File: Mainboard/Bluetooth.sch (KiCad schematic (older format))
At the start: 26 parts, among them J10 U.FL, J11 JST-PH 01x02, U10 BTM331

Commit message: Modify library references
As described in the README of the newly added libraries submodule.
Schematic and PCB are synced.

Hardware folder is renamed to mainboard
Any other PCBs can be put in their own subfolder in the gitrepo

Commit also swaps source/drain of Q1 because it appeared wrong for some
reason after updating all symbol/footprints.
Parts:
- J10: footprint ZOUDIOfootprints:Hirose_U.FL-R-SMT-1 -> ZOUDIO-footprints:Hirose_U.FL-R-SMT-1; symbol ZOUDIOsymbols:U.FL -> ZOUDIO-symbols:U.FL
- U10: footprint ZOUDIOfootprints:BTM331 -> ZOUDIO-footprints:BTM331; symbol ZOUDIOsymbols:BTM331 -> ZOUDIO-symbols:BTM331
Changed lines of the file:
@@
 $EndComp
 $Comp
-L ZOUDIOsymbols:BTM331 U10
+L ZOUDIO-symbols:BTM331 U10
 U 1 1 5FC5AF86
 P 4100 4100
+AR Path="/5FC5AF86" Ref="U10"  Part="1"
+AR Path="/60BB5CE1/5FC5AF86" Ref="U10"  Part="1"
 F 0 "U10" H 4100 4150 50  0000 C CNN
 F 1 "BTM331" H 4100 4050 50  0000 C CNN
-F 2 "ZOUDIOfootprints:BTM331" H 3650 4400 50  0001 C CNN
+F 2 "ZOUDIO-footprints:BTM331" H 3650 4400 50  0001 C CNN
 F 3 "" H 3650 4400 50  0001 C CNN
 F 4 "Tianjiarun" H 4100 4100 50  0001 C CNN "Manufacturer"
@@
 	2550 4850 2550 4900
 $Comp
-L ZOUDIOsymbols:U.FL J10
+L ZOUDIO-symbols:U.FL J10
 U 1 1 5FC5B37E
 P 3850 2350
 F 0 "J10" H 3850 2615 50  0000 C CNN
 F 1 "U.FL" H 3850 2524 50  0000 C CNN
-F 2 "ZOUDIOfootprints:Hirose_U.FL-R-SMT-1" H 3850 2350 50  0001 C CNN
+F 2 "ZOUDIO-footprints:Hirose_U.FL-R-SMT-1" H 3850 2350 50  0001 C CNN
 F 3 "" H 3850 2350 50  0001 C CNN
 F 4 "Hirose" H 3850 2350 50  0001 C CNN "Manufacturer"

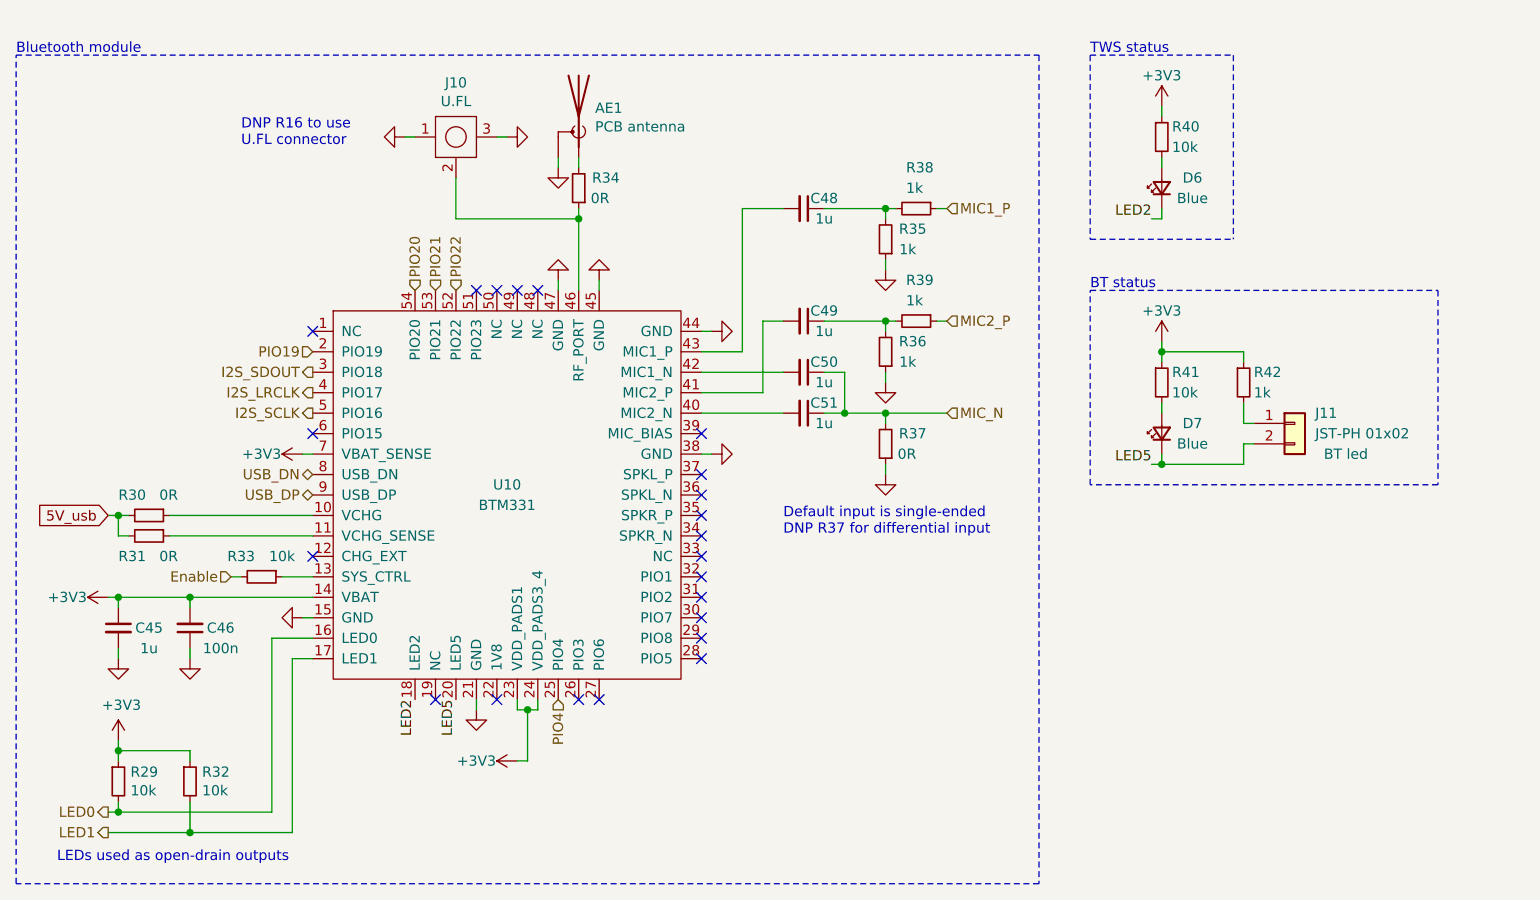
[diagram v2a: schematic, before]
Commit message: Before testing CH340B and VCHG
Cleaned up amp lay-out a bit in the meanwhile
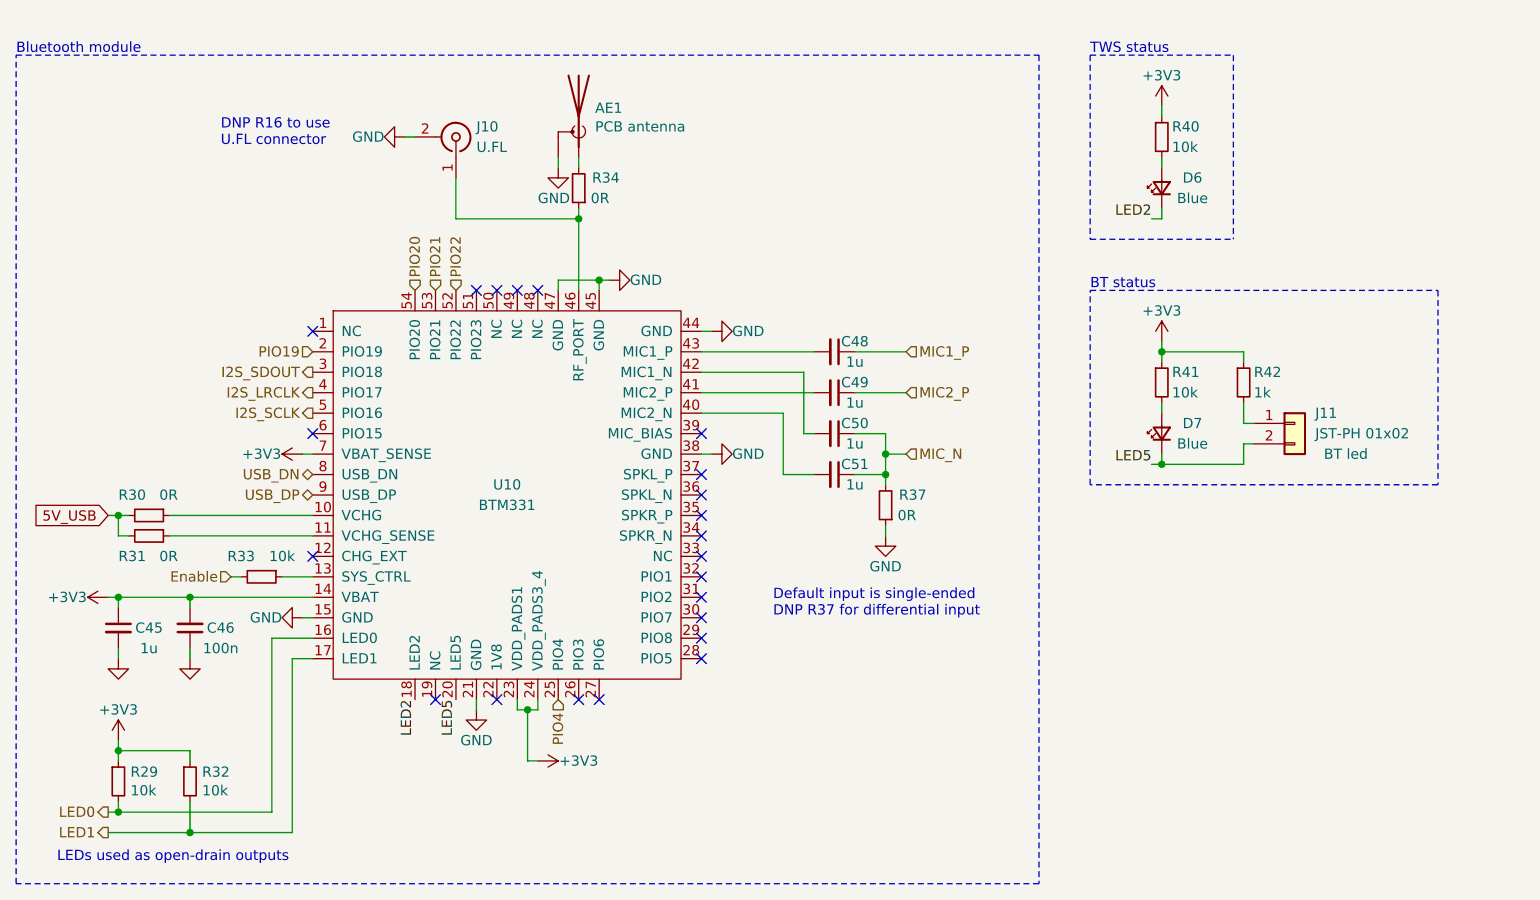
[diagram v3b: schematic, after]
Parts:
- removed J10: U.FL, ZOUDIO-footprints:Hirose_U.FL-R-SMT-1, symbol ZOUDIO-symbols:U.FL
- removed R35, R36, R38, R39: 1k, Resistor_SMD:R_0603_1608Metric, symbol Device:R_Small
- added J10: U.FL, Connector_Coaxial:U.FL_Hirose_U.FL-R-SMT-1_Vertical, symbol Connector:Conn_Coaxial
- AE1: Config DNP -> dnp; Partnumber virtual -> (none)
- C45, C48, C49, C50, C51: Manufacturer Yageo -> Taiyo Yuden; Partnumber CC0805KKX7R9BB105 -> UMK212B7105KG-T
- C46: Manufacturer Walsin -> Murata; Partnumber 0603B104J500CT -> GCM188L81H104KA57D
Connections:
- net GND: now also J10.2 (Ext)
- net MIC1_P: now also C48.1
- net MIC2_P: now also C49.1
- net at R34.1, U10.46 (RF_PORT): now also J10.1 (In)
- net 5V_usb renamed 5V_USB
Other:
- moved on the sheet: C48, C49, C50, C51, R37

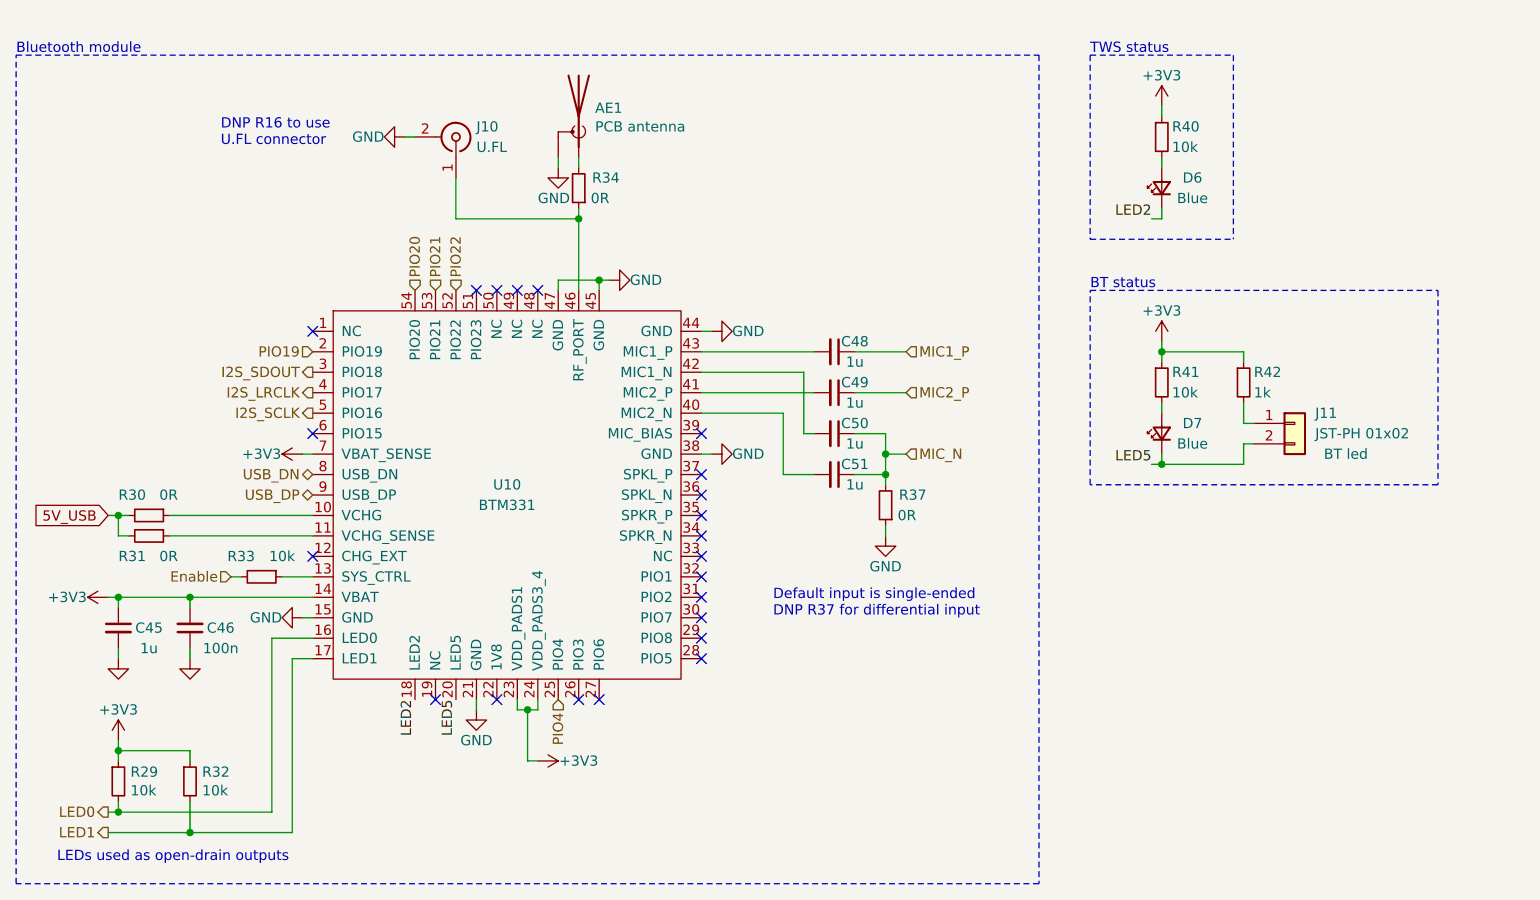
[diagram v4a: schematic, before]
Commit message: Mainboard: Version 1.0
Still need to clean up 3D models and BoM list,
but gerberexport-ready and ready to order.
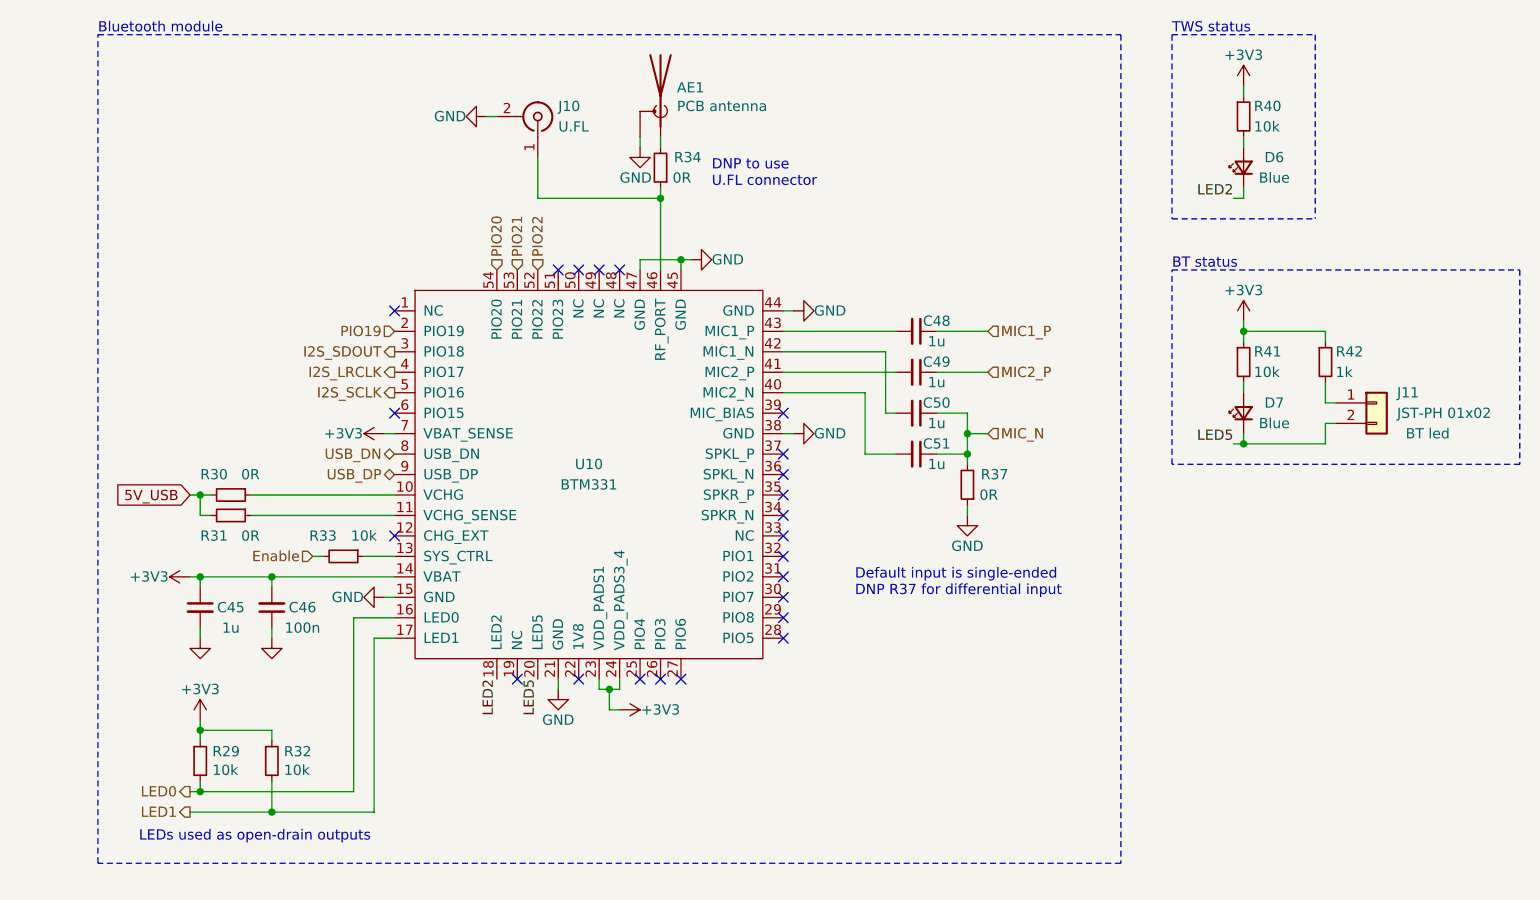
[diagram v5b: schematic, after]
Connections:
- net PIO4: no longer names the net of U10.25 (PIO4)
- no-connect marks 22 -> 23
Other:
- note added: "DNP to use \nU.FL connector"
- note removed: "DNP R16 to use \nU.FL connector"
- moved on the sheet: AE1, C45, C46, C48, C49, C50, C51, D6, D7, J10, J11, R29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

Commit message: Clean up schematic for BoM export
- Change 22u 0805's (amp decoupling) to 15u
- Change 680n 0805's (part of output filter) to 470n
- Change C1 (amp bulk cap) from 820u to 1000u
- Add BoM.ini for KiBom export and
- Complete fields needed for KiBom (Manufacturer and partnumber)
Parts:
- D6, D7: Manufacturer Orient -> Wurth; Partnumber ORH-B36G -> 150060BS75000
- J10: Manufacturer (none) -> Hirose; Partnumber (none) -> U.FL-R-SMT-1(10)
- J11: Manufacturer (none) -> JST; Partnumber (none) -> B2B-PH-K-S(LF)(SN)
- R29, R32, R33, R40, R41: Manufacturer Uni-royal -> Yageo; Partnumber 0603WAF1002T5E -> RC0603FR-0710KL
- R30, R31, R34, R37: Manufacturer Uni-royal -> Yageo; Partnumber 0603WAF0000T5E -> RC0603FR-070RL
- R42: Manufacturer Uni-royal -> Yageo; Partnumber 0603WAF1002T5E -> RC0603FR-071KL
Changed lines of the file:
@@
 F 2 "Resistor_SMD:R_0603_1608Metric" H 7700 3450 50  0001 C CNN
 F 3 "~" H 7700 3450 50  0001 C CNN
-F 4 "Uni-royal" H 7700 3450 50  0001 C CNN "Manufacturer"
-F 5 "0603WAF1002T5E" H 7700 3450 50  0001 C CNN "Partnumber"
+F 4 "Yageo" H 7700 3450 50  0001 C CNN "Manufacturer"
+F 5 "RC0603FR-0710KL" H 7700 3450 50  0001 C CNN "Partnumber"
 	1    7700 3450
 	1    0    0    -1
@@
 F 2 "LED_SMD:LED_0603_1608Metric" V 7700 3700 50  0001 C CNN
 F 3 "~" V 7700 3700 50  0001 C CNN
-F 4 "Orient" H 7700 3700 50  0001 C CNN "Manufacturer"
-F 5 "ORH-B36G" H 7700 3700 50  0001 C CNN "Partnumber"
+F 4 "Wurth" H 7700 3700 50  0001 C CNN "Manufacturer"
+F 5 "150060BS75000" H 7700 3700 50  0001 C CNN "Partnumber"
 	1    7700 3700
 	0    -1   -1   0
@@
 F 2 "Resistor_SMD:R_0603_1608Metric" H 4850 2500 50  0001 C CNN
 F 3 "~" H 4850 2500 50  0001 C CNN
-F 4 "Uni-royal" H 4850 2500 50  0001 C CNN "Manufacturer"
-F 5 "0603WAF0000T5E" H 4850 2500 50  0001 C CNN "Partnumber"
+F 4 "Yageo" H 4850 2500 50  0001 C CNN "Manufacturer"
+F 5 "RC0603FR-070RL" H 4850 2500 50  0001 C CNN "Partnumber"
 	1    4850 2500
 	-1   0    0    1
@@
 F 2 "Resistor_SMD:R_0603_1608Metric" H 7700 2250 50  0001 C CNN
 F 3 "~" H 7700 2250 50  0001 C CNN
-F 4 "Uni-royal" H 7700 2250 50  0001 C CNN "Manufacturer"
-F 5 "0603WAF1002T5E" H 7700 2250 50  0001 C CNN "Partnumber"
+F 4 "Yageo" H 7700 2250 50  0001 C CNN "Manufacturer"
+F 5 "RC0603FR-0710KL" H 7700 2250 50  0001 C CNN "Partnumber"
 	1    7700 2250
 	1    0    0    -1
@@
 F 2 "LED_SMD:LED_0603_1608Metric" V 7700 2500 50  0001 C CNN
 F 3 "~" V 7700 2500 50  0001 C CNN
-F 4 "Orient" H 7700 2500 50  0001 C CNN "Manufacturer"
-F 5 "ORH-B36G" H 7700 2500 50  0001 C CNN "Partnumber"
+F 4 "Wurth" H 7700 2500 50  0001 C CNN "Manufacturer"
+F 5 "150060BS75000" H 7700 2500 50  0001 C CNN "Partnumber"
 	1    7700 2500
 	0    -1   -1   0
@@
 F 2 "Resistor_SMD:R_0603_1608Metric" H 2600 5400 50  0001 C CNN
 F 3 "~" H 2600 5400 50  0001 C CNN
-F 4 "Uni-royal" H 2600 5400 50  0001 C CNN "Manufacturer"
-F 5 "0603WAF1002T5E" H 2600 5400 50  0001 C CNN "Partnumber"
+F 4 "Yageo" H 2600 5400 50  0001 C CNN "Manufacturer"
+F 5 "RC0603FR-0710KL" H 2600 5400 50  0001 C CNN "Partnumber"
 	1    2600 5400
 	1    0    0    -1
@@
 F 2 "Resistor_SMD:R_0603_1608Metric" H 2950 5400 50  0001 C CNN
 F 3 "~" H 2950 5400 50  0001 C CNN
-F 4 "Uni-royal" H 2950 5400 50  0001 C CNN "Manufacturer"
-F 5 "0603WAF1002T5E" H 2950 5400 50  0001 C CNN "Partnumber"
+F 4 "Yageo" H 2950 5400 50  0001 C CNN "Manufacturer"
+F 5 "RC0603FR-0710KL" H 2950 5400 50  0001 C CNN "Partnumber"
 	1    2950 5400
 	1    0    0    -1
@@
 F 2 "Resistor_SMD:R_0603_1608Metric" H 3300 4400 50  0001 C CNN
 F 3 "~" H 3300 4400 50  0001 C CNN
-F 4 "Uni-royal" H 3300 4400 50  0001 C CNN "Manufacturer"
-F 5 "0603WAF1002T5E" H 3300 4400 50  0001 C CNN "Partnumber"
+F 4 "Yageo" H 3300 4400 50  0001 C CNN "Manufacturer"
+F 5 "RC0603FR-0710KL" H 3300 4400 50  0001 C CNN "Partnumber"
 	1    3300 4400
 	0    1    1    0
@@
 F 3 "~" H 8350 3650 50  0001 C CNN
 F 4 "BT led" H 8600 3500 50  0000 C CNN "Function"
+F 5 "JST" H 8350 3650 50  0001 C CNN "Manufacturer"
+F 6 "B2B-PH-K-S(LF)(SN)" H 8350 3650 50  0001 C CNN "Partnumber"
 	1    8350 3650
 	1    0    0    -1
@@
 F 2 "Resistor_SMD:R_0603_1608Metric" H 8100 3450 50  0001 C CNN
 F 3 "~" H 8100 3450 50  0001 C CNN
-F 4 "Uni-royal" H 8100 3450 50  0001 C CNN "Manufacturer"
-F 5 "0603WAF1002T5E" H 8100 3450 50  0001 C CNN "Partnumber"
+F 4 "Yageo" H 8100 3450 50  0001 C CNN "Manufacturer"
+F 5 "RC0603FR-071KL" H 8100 3450 50  0001 C CNN "Partnumber"
 	1    8100 3450
 	1    0    0    -1
@@
 F 2 "Resistor_SMD:R_0603_1608Metric" H 6350 4050 50  0001 C CNN
 F 3 "~" H 6350 4050 50  0001 C CNN
-F 4 "Uni-royal" H 6350 4050 50  0001 C CNN "Manufacturer"
-F 5 "0603WAF0000T5E" H 6350 4050 50  0001 C CNN "Partnumber"
+F 4 "Yageo" H 6350 4050 50  0001 C CNN "Manufacturer"
+F 5 "RC0603FR-070RL" H 6350 4050 50  0001 C CNN "Partnumber"
 	1    6350 4050
 	-1   0    0    1
@@
 F 2 "Connector_Coaxial:U.FL_Hirose_U.FL-R-SMT-1_Vertical" H 4250 2250 50  0001 C CNN
 F 3 " ~" H 4250 2250 50  0001 C CNN
+F 4 "Hirose" H 4250 2250 50  0001 C CNN "Manufacturer"
+F 5 "U.FL-R-SMT-1(10)" H 4250 2250 50  0001 C CNN "Partnumber"
 	1    4250 2250
 	0    1    -1   0
@@
 F 2 "Resistor_SMD:R_0603_1608Metric" H 2750 4100 50  0001 C CNN
 F 3 "~" H 2750 4100 50  0001 C CNN
-F 4 "Uni-royal" H 2750 4100 50  0001 C CNN "Manufacturer"
-F 5 "0603WAF0000T5E" H 2750 4100 50  0001 C CNN "Partnumber"
+F 4 "Yageo" H 2750 4100 50  0001 C CNN "Manufacturer"
+F 5 "RC0603FR-070RL" H 2750 4100 50  0001 C CNN "Partnumber"
 	1    2750 4100
 	0    1    1    0
@@
 F 2 "Resistor_SMD:R_0603_1608Metric" H 2750 4200 50  0001 C CNN
 F 3 "~" H 2750 4200 50  0001 C CNN
-F 4 "Uni-royal" H 2750 4200 50  0001 C CNN "Manufacturer"
-F 5 "0603WAF0000T5E" H 2750 4200 50  0001 C CNN "Partnumber"
+F 4 "Yageo" H 2750 4200 50  0001 C CNN "Manufacturer"
+F 5 "RC0603FR-070RL" H 2750 4200 50  0001 C CNN "Partnumber"
 	1    2750 4200
 	0    1    1    0
